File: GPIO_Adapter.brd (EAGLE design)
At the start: 160 x 100 mm, 1 part

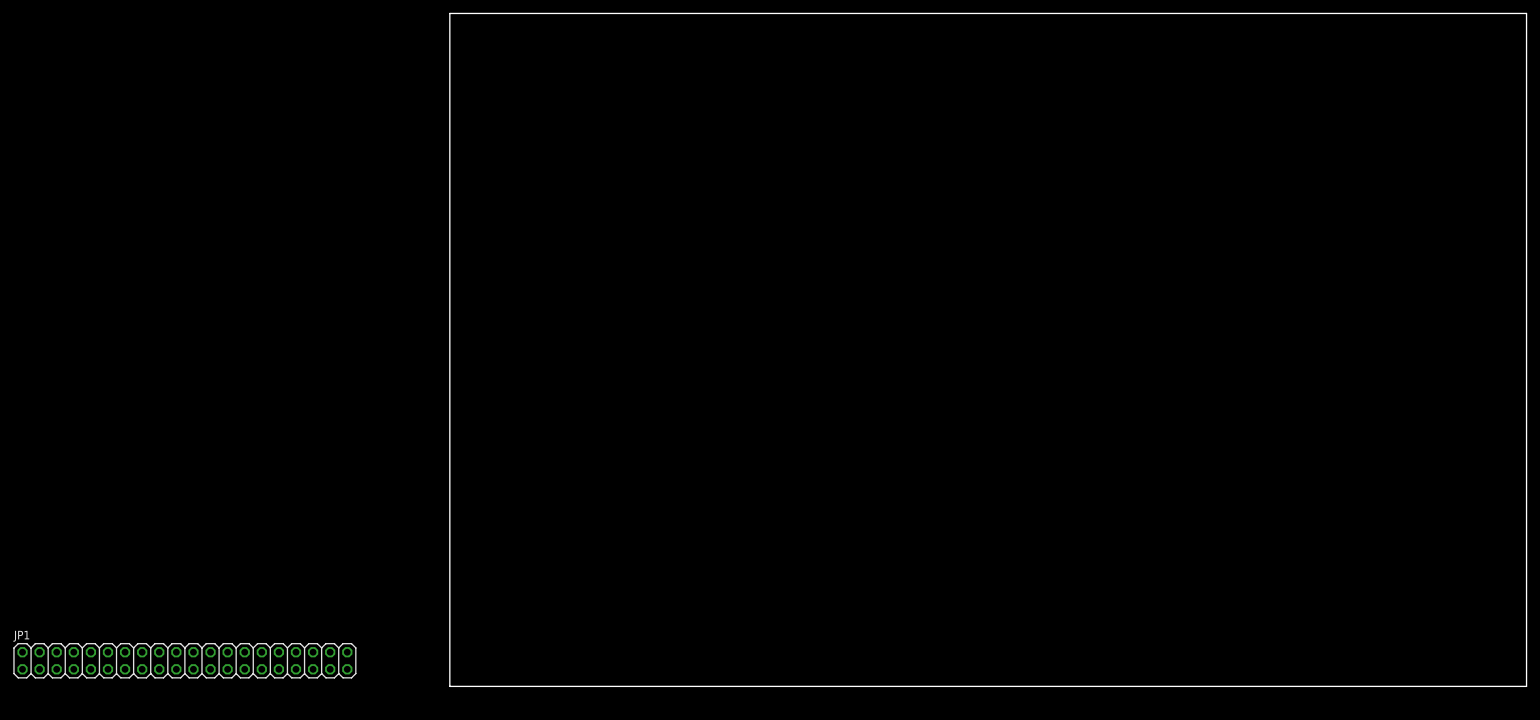
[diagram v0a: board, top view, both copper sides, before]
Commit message: GPIO got terminal blocks
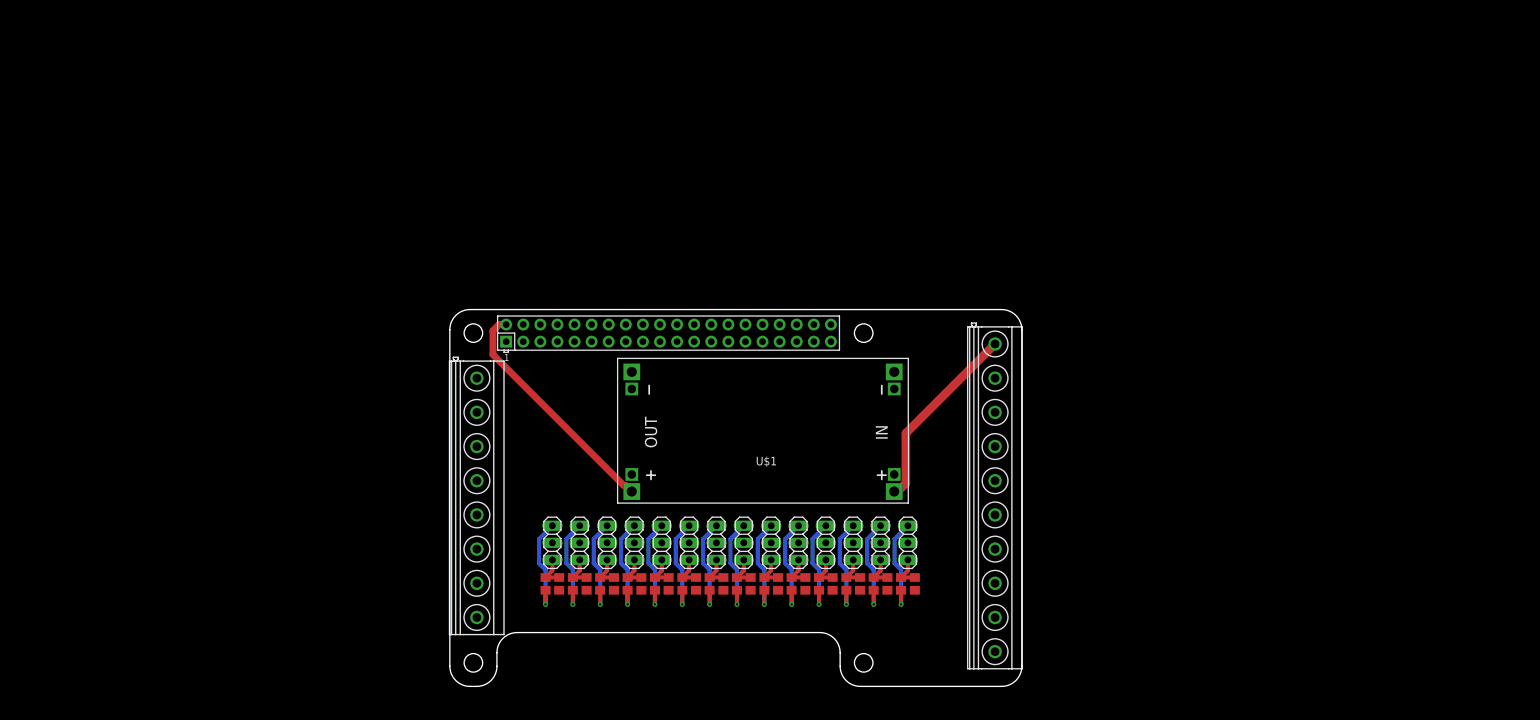
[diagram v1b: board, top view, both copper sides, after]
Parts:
- added JP10, JP11, JP12, JP13, JP14, JP15, JP3, JP4, JP5, JP6, JP7, JP8, JP9: (no value), pinhead:1X03
- added R1, R11, R13, R15, R17, R19, R21, R23, R25, R27, R29, R5, R7, R9: 7k5, rcl:R0805
- added R10, R12, R14, R16, R18, R2, R20, R22, R24, R26, R28, R30, R6, R8: 2k7, rcl:R0805
- added U$1: DC-DC-STEP-DOWN-LM2596HVS, diy-modules:DC-DC-STEP-DOWN-LM2596HVS
- added X1: RASPI_BOARD_B+#_F, raspberrypi_bastelstube_v13:RASPI_BOARD_B+_FULL
- added X2: MKDSN1,5/8-5,08, con-phoenix-508:MKDSN1,5/8-5,08
- added X3: MKDSN1,5/10-5,08, con-phoenix-508:MKDSN1,5/10-5,08
- JP1: device pinhead:2X20 -> pinhead:1X03
- moved JP1 57.4 mm to (15.2, 21.3), turned to 270 degrees
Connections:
- removed net N$19: JP1.37
- removed net N$20 (its old number): JP1.39
- new net 3,3V: X1.1, X1.17
- new net 5VDC: U$1.OUT+, X1.2, X1.4
- new net GND: R10.2, R12.2, R14.2, R16.2, R18.2, R2.2, R20.2, R22.2, R24.2, R26.2, R28.2, R30.2, R6.2, R8.2, U$1.IN-, U$1.OUT-, X1.14, X1.20, X1.25, X1.30, X1.34, X1.39, X1.6, X1.9, X3.2
- new net N$40: JP9.3, R17.2, R18.1
- new net N$41: JP9.2
- new net N$42: JP10.1, R19.1
- new net N$43: JP10.3, R19.2, R20.1
- new net N$44: JP10.2
- new net N$45: JP11.1, R21.1
- new net N$46: JP11.3, R21.2, R22.1
- new net N$47: JP11.2
- new net N$48: JP12.1, R23.1
- new net N$49: JP12.3, R23.2, R24.1
- new net N$50: JP12.2
- new net N$51: JP13.1, R25.1
- new net N$52: JP13.3, R25.2, R26.1
- new net N$53: JP13.2
- new net N$54: JP14.1, R27.1
- new net N$55: JP14.3, R27.2, R28.1
- new net N$56: JP14.2
- new net N$57: JP15.1, R29.1
- new net N$58: JP15.3, R29.2, R30.1
- new net N$59: JP15.2
- new net VIN: U$1.IN+, X3.1
- net N$1: now also X2.1; no longer JP1.1
- net N$10: now also JP1.3, R1.2, R2.1; no longer JP1.19
- net N$11: now also X3.3; no longer JP1.21
- net N$12: now also X3.4; no longer JP1.23
- net N$13: now also X3.5; no longer JP1.25
- net N$14: now also X3.6; no longer JP1.27
- net N$15: now also X3.7; no longer JP1.29
- net N$16: now also X3.8; no longer JP1.31
- net N$17: now also X3.9; no longer JP1.33
- net N$18: now also X3.10; no longer JP1.35
- net N$2: now also X2.2; no longer JP1.3
- net N$21: now also JP3.1, R5.1; no longer JP1.40
- net N$22: now also JP3.3, R5.2, R6.1; no longer JP1.38
- net N$23: now also JP3.2; no longer JP1.36
- net N$24: now also JP4.1, R7.1; no longer JP1.34
- net N$25: now also JP4.3, R7.2, R8.1; no longer JP1.32
- net N$26: now also JP4.2; no longer JP1.30
- net N$27: now also JP5.1, R9.1; no longer JP1.28
- net N$28: now also JP5.3, R10.1, R9.2; no longer JP1.26
- net N$29: now also JP5.2; no longer JP1.24
- net N$3: now also X2.3; no longer JP1.5
- net N$30: now also JP6.1, R11.1; no longer JP1.22
- net N$31: now also JP6.3, R11.2, R12.1; no longer JP1.20
- net N$32: now also JP6.2; no longer JP1.18
- net N$33: now also JP7.1, R13.1; no longer JP1.16
- net N$34: now also JP7.3, R13.2, R14.1; no longer JP1.14
- net N$35: now also JP7.2; no longer JP1.12
- net N$36: now also JP8.1, R15.1; no longer JP1.10
- net N$37: now also JP8.3, R15.2, R16.1; no longer JP1.8
- net N$38: now also JP8.2; no longer JP1.6
- net N$39: now also JP9.1, R17.1; no longer JP1.4
- net N$4: now also X2.4; no longer JP1.7
- net N$5: now also X2.5; no longer JP1.9
- net N$6: now also X2.6; no longer JP1.11
- net N$7: now also X2.7; no longer JP1.13
- net N$8: now also X2.8; no longer JP1.15
- net N$9: now also JP1.1, R1.1; no longer JP1.17
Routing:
- net 5VDC: track 0.00 -> 35.0 mm
- net VIN: track 0.00 -> 28.4 mm
- net N$9: track 0.00 -> 15.0 mm, vias 0 -> 1
- net N$57: track 0.00 -> 15.0 mm, vias 0 -> 1
- net N$54: track 0.00 -> 15.0 mm, vias 0 -> 1
- net N$48: track 0.00 -> 15.0 mm, vias 0 -> 1
- net N$45: track 0.00 -> 15.0 mm, vias 0 -> 1
- net N$42: track 0.00 -> 15.0 mm, vias 0 -> 1
- net N$39: track 0.00 -> 15.0 mm, vias 0 -> 1
- net N$36: track 0.00 -> 15.0 mm, vias 0 -> 1
- net N$33: track 0.00 -> 15.0 mm, vias 0 -> 1
- net N$30: track 0.00 -> 15.0 mm, vias 0 -> 1
- net N$27: track 0.00 -> 15.0 mm, vias 0 -> 1
- net N$24: track 0.00 -> 15.0 mm, vias 0 -> 1
- net N$21: track 0.00 -> 15.0 mm, vias 0 -> 1
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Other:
- board size 160 x 100 mm -> 85 x 56 mm

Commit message: GPIO board ready for manufactoring
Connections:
- removed net 3,3V: X1.1, X1.17
- removed net N$1: X2.1
- removed net N$10: JP1.3, R1.2, R2.1
- removed net N$11: X3.3
- removed net N$12: X3.4
- removed net N$13: X3.5
- removed net N$14: X3.6
- removed net N$15: X3.7
- removed net N$16: X3.8
- removed net N$17: X3.9
- removed net N$18: X3.10
- removed net N$2: X2.2
- removed net N$20: JP1.2
- removed net N$22: JP3.3, R5.2, R6.1
- removed net N$23: JP3.2
- removed net N$25: JP4.3, R7.2, R8.1
- removed net N$26: JP4.2
- removed net N$28: JP5.3, R10.1, R9.2
- removed net N$29: JP5.2
- removed net N$3: X2.3
- removed net N$31: JP6.3, R11.2, R12.1
- removed net N$32: JP6.2
- removed net N$34: JP7.3, R13.2, R14.1
- removed net N$35: JP7.2
- removed net N$37: JP8.3, R15.2, R16.1
- removed net N$38: JP8.2
- removed net N$4: X2.4
- removed net N$40: JP9.3, R17.2, R18.1
- removed net N$41: JP9.2
- removed net N$43: JP10.3, R19.2, R20.1
- removed net N$44: JP10.2
- removed net N$46: JP11.3, R21.2, R22.1
- removed net N$47: JP11.2
- removed net N$49: JP12.3, R23.2, R24.1
- removed net N$5: X2.5
- removed net N$50: JP12.2
- removed net N$52: JP13.3, R25.2, R26.1
- removed net N$53: JP13.2
- removed net N$55: JP14.3, R27.2, R28.1
- removed net N$56: JP14.2
- removed net N$58: JP15.3, R29.2, R30.1
- removed net N$59: JP15.2
- removed net N$6: X2.6
- removed net N$7: X2.7
- removed net N$8: X2.8
- new net 3.3V: X1.1, X1.17, X2.2
- new net GPIO12: JP5.3, R10.1, R9.2, X1.32
- new net GPIO12EXT: JP5.2, X3.6
- new net GPIO13: JP6.3, R11.2, R12.1, X1.33
- new net GPIO13EXT: JP6.2, X3.7
- new net GPIO16: JP7.3, R13.2, R14.1, X1.36
- new net GPIO16EXT: JP7.2, X3.8
- new net GPIO17: JP8.3, R15.2, R16.1, X1.11
- new net GPIO17EXT: JP8.2, X3.9
- new net GPIO18: JP9.3, R17.2, R18.1, X1.12
- new net GPIO18EXT: JP9.2, X3.10
- new net GPIO19: JP10.3, R19.2, R20.1, X1.35
- new net GPIO19EXT: JP10.2, X2.3
- new net GPIO20: JP12.3, R23.2, R24.1, X1.38
- new net GPIO20EXT: JP12.2, X2.4
- new net GPIO22: JP14.3, R27.2, R28.1, X1.15
- new net GPIO22EXT: JP14.2, X2.5
- new net GPIO24: JP11.3, R21.2, R22.1, X1.18
- new net GPIO24EXT: JP11.2, X2.6
- new net GPIO26: JP13.3, R25.2, R26.1, X1.37
- new net GPIO26EXT: JP13.2, X2.7
- new net GPIO27: JP15.3, R29.2, R30.1, X1.13
- new net GPIO27EXT: JP15.2, X2.8
- new net GPIO4: JP1.3, R1.2, R2.1, X1.7
- new net GPIO4EXT: JP1.2, X3.3
- new net GPIO5: JP3.3, R5.2, R6.1, X1.29
- new net GPIO5EXT: JP3.2, X3.4
- new net GPIO6: JP4.3, R7.2, R8.1, X1.31
- new net GPIO6EXT: JP4.2, X3.5
- new net N$75: X1.40
- new net N$76: X1.5
- new net N$77: X1.3
- net 5VDC: now also X2.1
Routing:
- net GND: track 0.00 -> 201.3 mm, vias 0 -> 16
- net GPIO27EXT: track 0.00 -> 107.1 mm, vias 0 -> 3
- net GPIO26EXT: track 0.00 -> 88.8 mm
- net GPIO6EXT: track 0.00 -> 85.3 mm
- net GPIO5EXT: track 0.00 -> 82.6 mm, vias 0 -> 2
- net GPIO17: track 0.00 -> 81.9 mm
- net GPIO4EXT: track 0.00 -> 80.2 mm
- net GPIO18: track 0.00 -> 77.9 mm, vias 0 -> 1
- net GPIO22EXT: track 0.00 -> 73.1 mm, vias 0 -> 2
- net GPIO27: track 0.00 -> 72.0 mm, vias 0 -> 1
- net GPIO12EXT: track 0.00 -> 71.6 mm
- net GPIO20EXT: track 0.00 -> 71.1 mm, vias 0 -> 2
- net GPIO19EXT: track 0.00 -> 69.9 mm, vias 0 -> 2
- net GPIO24EXT: track 0.00 -> 68.1 mm, vias 0 -> 2
- net GPIO22: track 0.00 -> 68.1 mm, vias 0 -> 1
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- added copper zone on layer 1, net GND
- added copper zone on layer 16, net GND
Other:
- board text added: "12"
- board text added: "13"
- board text added: "16"
- board text added: "17"
- board text added: "18"
- board text added: "19"
- board text added: "20"
- board text added: "22"
- board text added: "24"
- board text added: "26"
- board text added: "27"
- board text added: "3.3V"
- board text added: "4"
- board text added: "5"
- board text added: "5-72V"
- board text added: "5V"
- board text added: "6"
- board text added: "GND"
- board text added: "GPIO12"
- board text added: "GPIO13"
- board text added: "GPIO16"
- board text added: "GPIO17"
- board text added: "GPIO18"
- board text added: "GPIO19"
- board text added: "GPIO20"
- board text added: "GPIO24"
- board text added: "GPIO26"
- board text added: "GPIO27"
- board text added: "GPIO4"
- board text added: "GPIO5"
- board text added: "GPIO6"
- board text added: "VIN"
